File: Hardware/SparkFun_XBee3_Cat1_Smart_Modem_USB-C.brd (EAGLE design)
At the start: 53.3 x 59.7 mm, 105 parts, among them J3 USB Female Type C Connector, J4 QWIIC_RIGHT_ANGLE, U2 AP63203, U5 ESD Diode, U6 CP210X

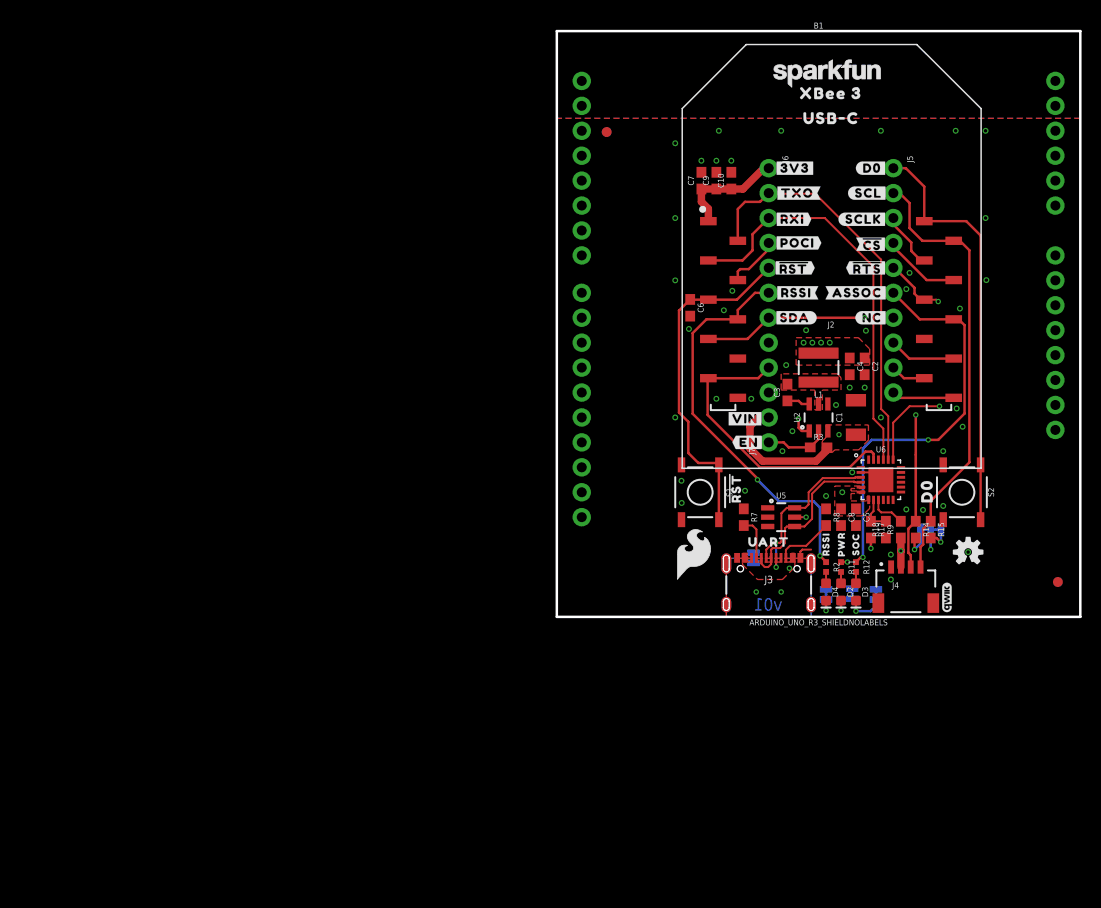
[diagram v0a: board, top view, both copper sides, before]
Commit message: General placement of parts
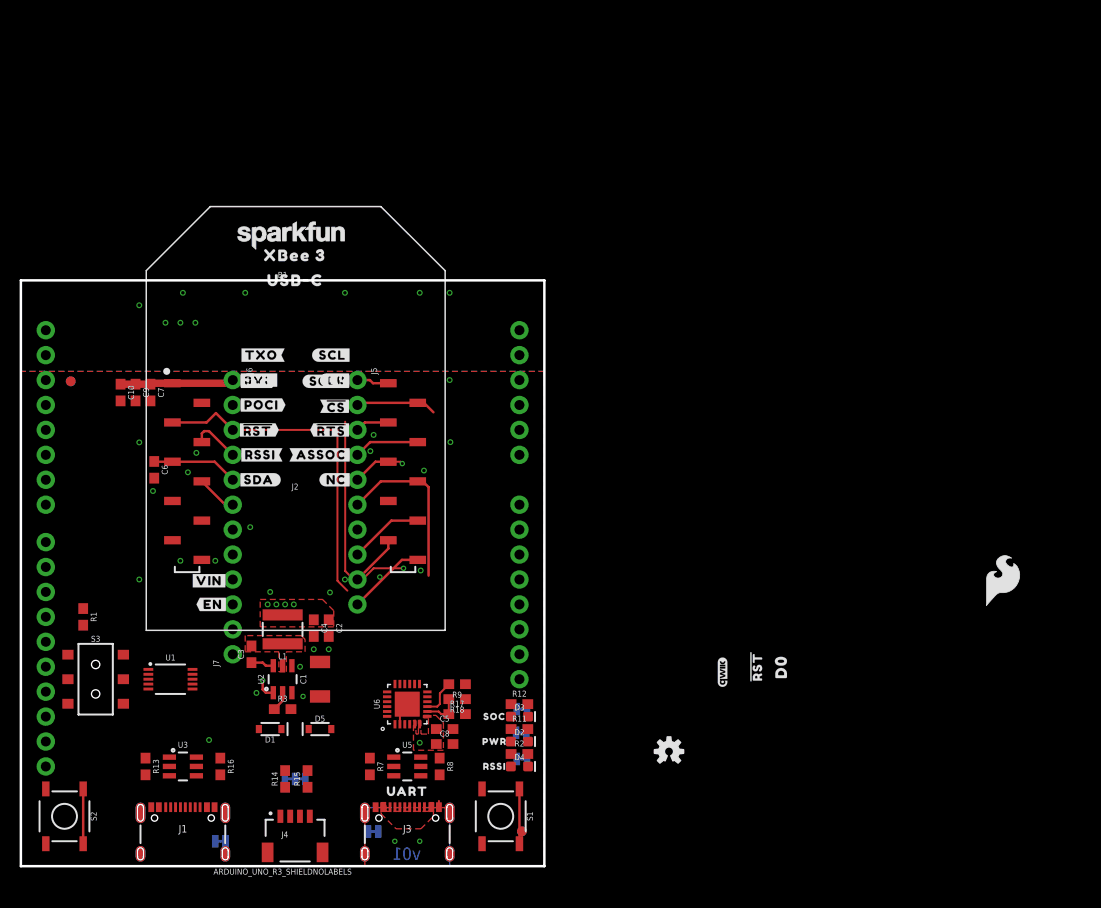
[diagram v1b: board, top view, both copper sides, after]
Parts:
- added D1, D5: 3A/10V/280mV, SparkFun-DiscreteSemi:SOD-323
- added J1: USB Female Type C Connector, SparkFun-Connectors:USB-C-16P-4LAYER-ISOLATED
- added R1: 100k, SparkFun-Resistors:0603
- added R13, R16: 5.1k, SparkFun-Resistors:0603
- added S3: (no value), SparkFun-Switches:SWITCH_DPDT_SMD_AYZ0202
- added SHLD1: JUMPER-SMT_2_NC_TRACE_SILK, SparkFun-Jumpers:SMT-JUMPER_2_NC_TRACE_SILK
- added U1: FSUSB30MUX_MSOP10, SparkFun-IC-Special-Function:MSOP10
- added U3: ESD Diode, SparkFun-DiscreteSemi:SOT-23-6
- R11, R12, R2: device SparkFun-Resistors:0402-TIGHT -> SparkFun-Resistors:0603
- moved S2 97.2 mm to (4.45, 5.08)
- moved I2C_PU 69.6 mm to (27.9, 8.89)
- moved U$26 69.6 mm to (27.9, 7.24)
- moved R14 69.1 mm to (26.9, 8.89), turned to 90 degrees
- moved R15 68.4 mm to (29.2, 8.89), turned to 90 degrees
- moved J4 67.2 mm to (27.9, 5.08)
- moved C10 65.9 mm to (10.2, 48.3), turned to 270 degrees
- moved C9 63.0 mm to (11.7, 48.3), turned to 270 degrees
- moved C1 60.8 mm to (30.5, 19.1)
- moved C2 60.8 mm to (31.4, 24.3)
- moved C3 60.8 mm to (23.5, 21.6)
- moved C4 60.8 mm to (29.8, 24.3)
- moved L1 60.8 mm to (26.7, 24.1)
- moved R3 60.8 mm to (26.7, 16.0)
- moved U2 60.8 mm to (26.7, 19.1)
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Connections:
- removed net N$17: B1.D12
- removed net N$20: B1.D9
- removed net N$22: B1.D8
- removed net N$24: B1.D7
- removed net N$25: B1.D6
- removed net N$4: J2.8
- new net DIRECT_D+: J1.A6, J1.B6, U1.3, U3.6
- new net DIRECT_D-: J1.A7, J1.B7, U1.7, U3.4
- new net DIRECT_SELECT: S3.2, S3.5, U1.1
- new net FIRMWARE: R1.2, S3.1, S3.4
- new net N$14: J1.B5, R16.2
- new net N$15: J1.A5, R13.2
- new net SHLD1: J1.SHLD1, J1.SHLD2, J1.SHLD3, J1.SHLD4, J1.SHLD5, J1.SHLD6, J1.SHLD7, J1.SHLD8, SHLD1.2
- new net V_USB_2: D1.A, J1.VBUS1, J1.VBUS2, U3.5
- new net XBEE_D+/SDA: J2.7, U1.4
- new net XBEE_D-: J2.8, U1.6
- net 3.3V: now also R1.1, U1.10
- net D11/SDA: now also U1.2; no longer J2.7
- net D12/SPI_POCI: now also B1.D12
- net D6/!RTS!: now also B1.D6
- net D7/!CTS!: now also B1.D7
- net D8/!DTR!: now also B1.D8
- net D9/!SLEEP!: now also B1.D9
- net GND: now also J1.GND, J1.GND2, R13.1, R16.1, S3.3, S3.6, SHLD1.1, U1.5, U1.9, U3.2
- net VIN: now also D1.C, D5.C
- net V_USB: now also D5.A
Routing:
- net D10/RSSI_PWM: track 53.1 -> 4.14 mm, vias 2 -> 0
- net D5/ASSOCIATE: track 58.2 -> 17.5 mm, vias 2 -> 0
- net D11/SDA: track 54.1 -> 13.9 mm, vias 2 -> 1
- net D1/SCL: track 46.0 -> 8.25 mm
- net D0: track 42.7 -> 8.87 mm
- net D8/!DTR!: track 30.8 -> 0.10 mm
- net D13/TXO: track 42.0 -> 16.2 mm
- net !RESET!: track 35.1 -> 14.6 mm
- net D+: track 19.5 -> 0.04 mm, vias 2 -> 0
- net VIN: track 29.3 -> 11.0 mm, vias 2 -> 1
- net D-: track 17.9 -> 0.15 mm
- net V_USB: track 7.08 -> 0.00 mm, vias 2 -> 0
- net D14/RXI: track 41.7 -> 34.7 mm
- net N$5: track 5.96 -> 0.00 mm
- net 3.3V: track 27.1 -> 21.7 mm, vias 9 -> 6
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- removed copper zone on layer 1, net VIN

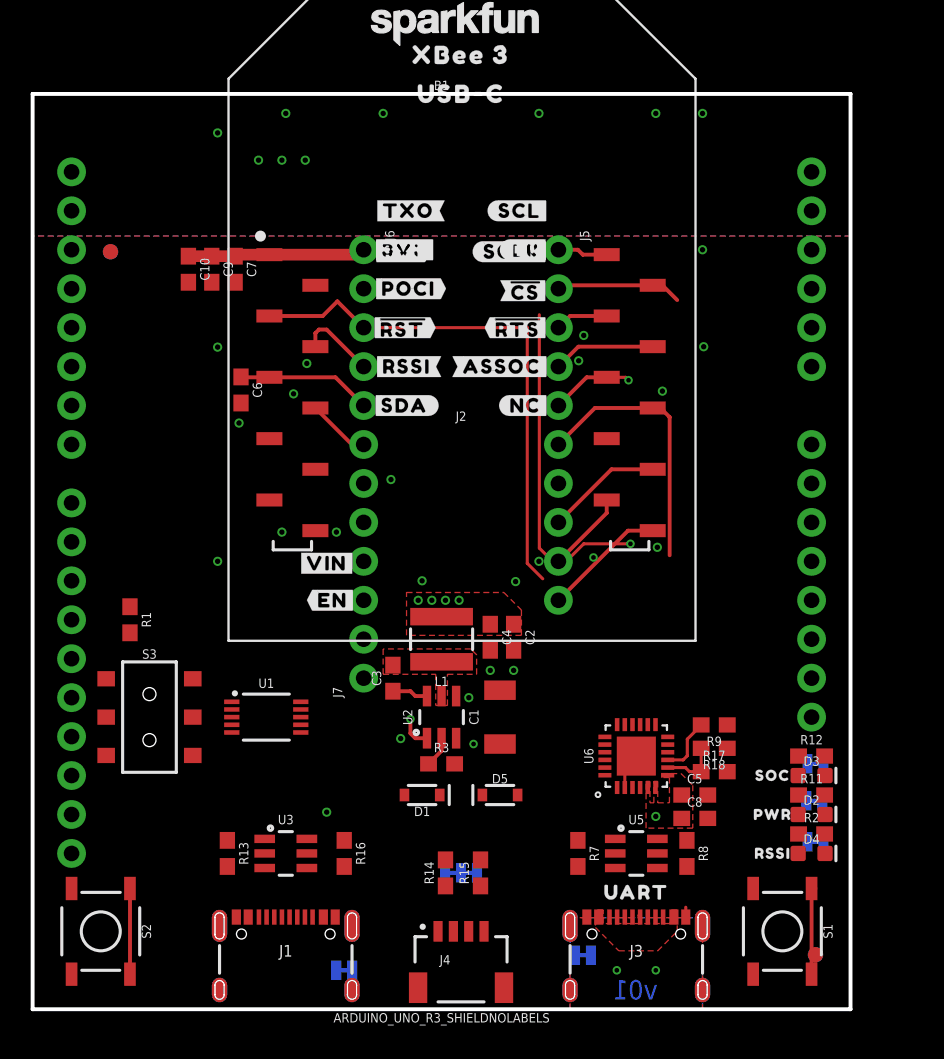
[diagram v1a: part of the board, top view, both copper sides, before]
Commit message: More changes to part placement
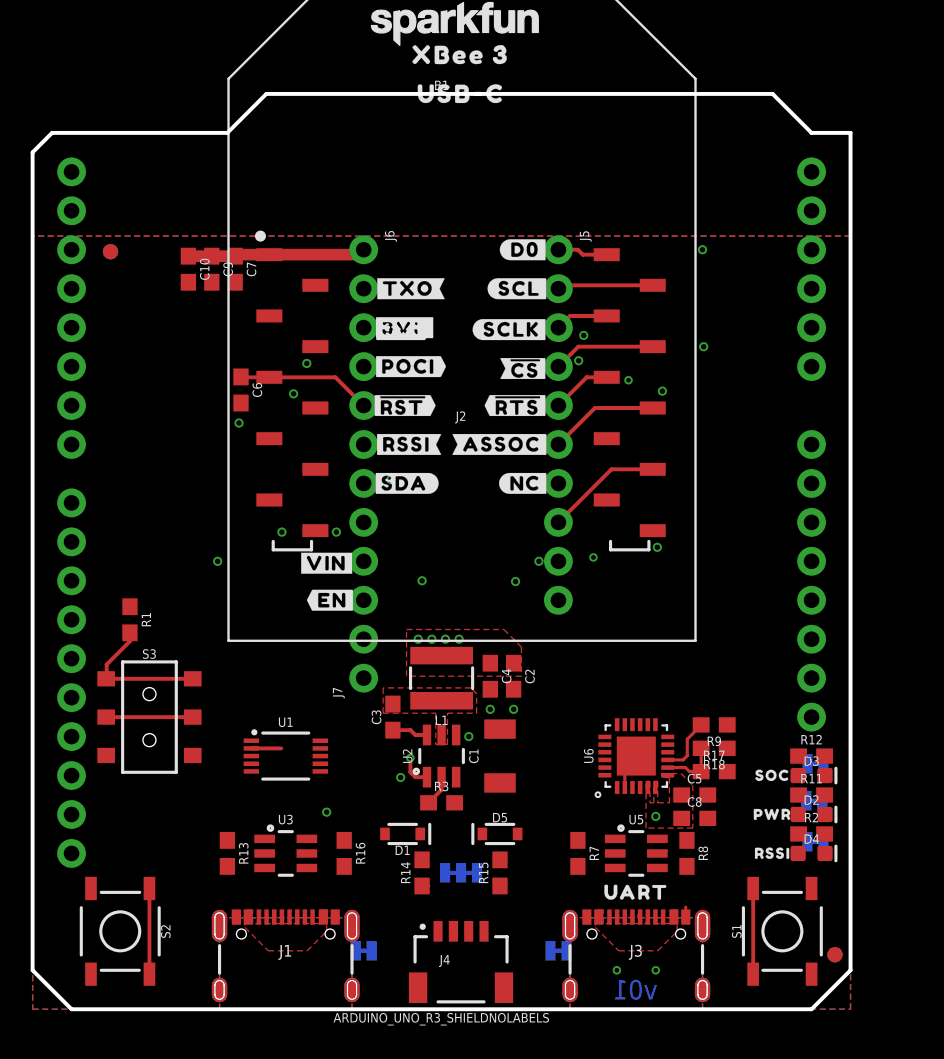
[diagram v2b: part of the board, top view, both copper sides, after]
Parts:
- moved U$45 5.08 mm to (24.5, 41.9)
- moved U$54 5.08 mm to (24.1, 39.4)
- moved U$58 5.08 mm to (31.6, 39.4)
- moved U$10 5.08 mm to (32.1, 34.3)
- moved U$21 5.08 mm to (24.5, 47.0)
- moved U$27 5.08 mm to (24.0, 44.3)
- moved U$55 5.08 mm to (24.4, 36.8)
- moved U$56 5.08 mm to (24.3, 34.3)
- moved U$57 5.08 mm to (30.6, 36.8)
- moved U$59 5.08 mm to (32.1, 41.8)
- moved U$60 5.08 mm to (31.2, 44.3)
- moved U$64 5.08 mm to (31.8, 47.0)
- moved U$9 5.08 mm to (24.3, 44.5)
- moved D1 2.84 mm to (24.1, 11.4)
- moved U1 2.84 mm to (16.5, 16.5)
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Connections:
- net N$27 renamed D4_SPI_PICO
- removed net N$16: B1.D13
- removed net N$28: B1.D3
- removed net N$29: B1.D2
- removed net N$35: B1.AREF
- removed net N$37: B1.5V
- removed net N$38: B1.VIN
- removed net N$39: B1.RES
- removed net N$40: B1.IOREF
- removed net N$41: B1.A5
- removed net N$42: B1.A4
- removed net N$43: B1.A3
- removed net N$44: B1.A2
- removed net N$45: B1.A1
- removed net N$46: B1.A0
- net D0: now also B1.A0
- net D11/SDA: no longer B1.D11
- net D2/SPI_CLK: now also B1.D2
- net D3/SPI_!CS!: now also B1.D3
- net VIN: now also B1.VIN
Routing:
- net D14/RXI: track 34.7 -> 0.00 mm
- net D6/!RTS!: track 21.5 -> 3.91 mm, vias 2 -> 1
- net D13/TXO: track 16.2 -> 0.00 mm
- net D11/SDA: track 13.9 -> 2.37 mm
- net VIN: track 11.0 -> 0.00 mm, vias 1 -> 0
- net D5/ASSOCIATE: track 17.5 -> 7.64 mm
- net FIRMWARE: track 0.00 -> 9.37 mm
- net D4/SPI_PICO: track 8.03 -> 0.00 mm
- net 3.3V: track 21.7 -> 13.8 mm
- net DIRECT_SELECT: track 0.00 -> 5.65 mm
- net D7/!CTS!: track 5.30 -> 0.00 mm
- net D12/SPI_POCI: track 5.13 -> 0.00 mm
- net D10/RSSI_PWM: track 4.14 -> 0.77 mm
- net D1/SCL: track 8.25 -> 6.89 mm
- net GND: vias 31 -> 21
- added copper zone on layer 1, net SHLD1
- added copper zone on layer 16, net SHLD1
- added copper zone on layer 1, net V_USB_2
- removed copper zone on layer 15, net 3.3V
- removed copper zone on layer 2, net GND
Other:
- outline, holes or cut-outs redrawn

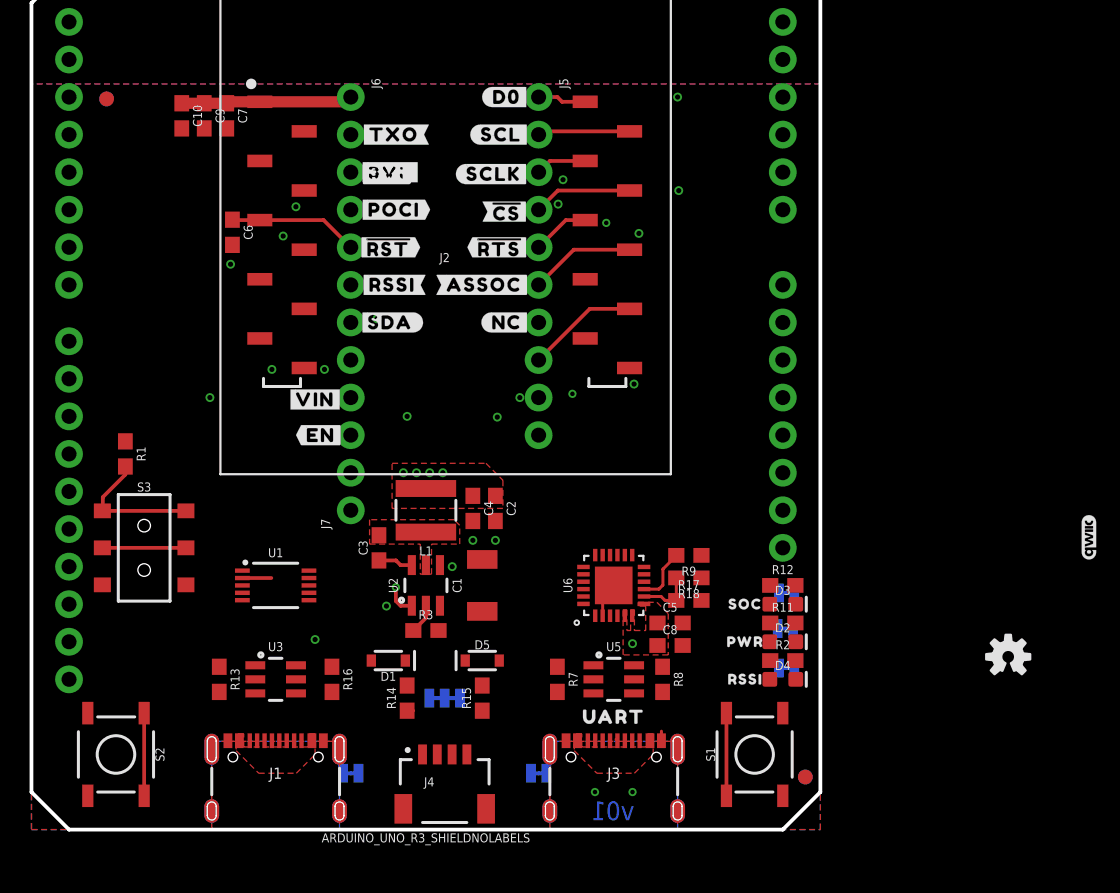
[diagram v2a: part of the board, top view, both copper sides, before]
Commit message: Rearranges USB-C and Qwiic connectors
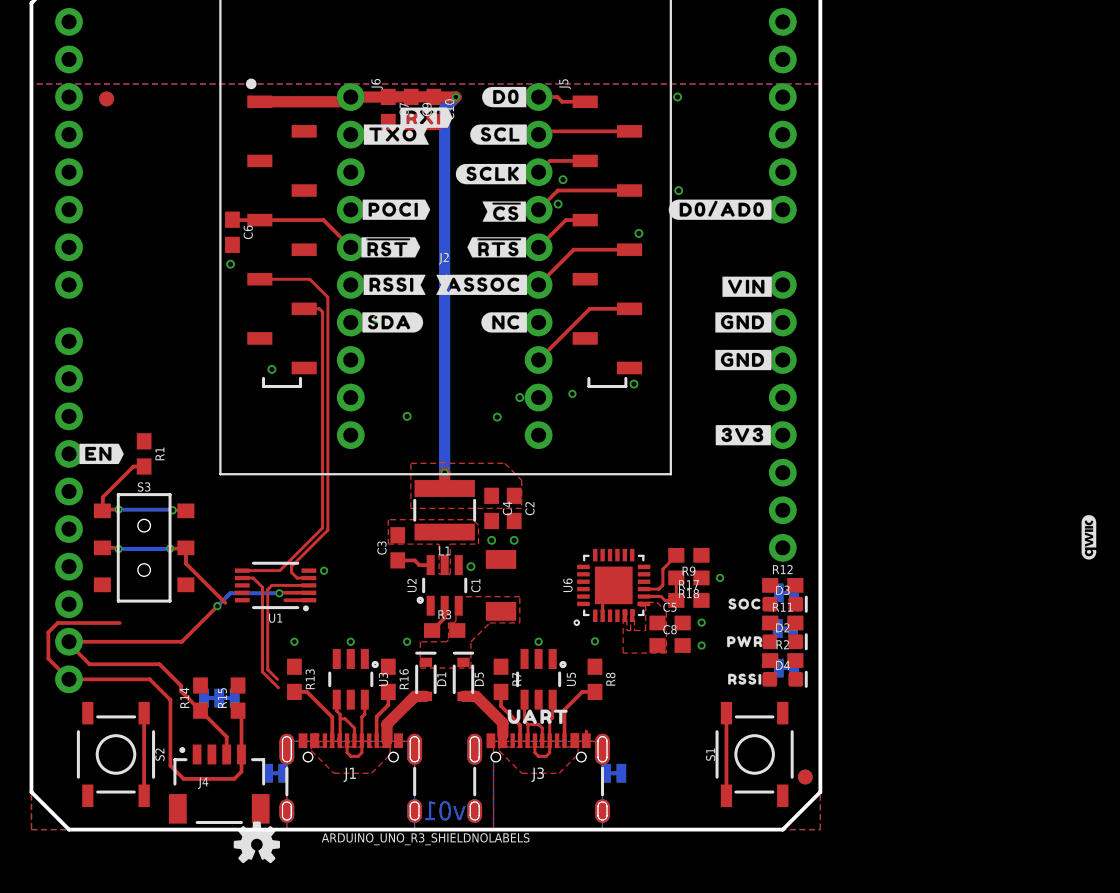
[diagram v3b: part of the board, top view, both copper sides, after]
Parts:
- removed J7: (no value), SparkFun-Connectors:1X02_NO_SILK
- removed U$46: (no value), top:#VIN#4
- removed U$67: (no value), botmirror:#EN#15
- removed U$9: (no value), top:#3V3#1
- added U$29: (no value), topmirror:#GND#0
- moved LOGO2 52.4 mm to (15.2, -1.02)
- moved U$44 40.4 mm to (48.1, 26.7), flipped to the top
- moved U$66 30.2 mm to (48.4, 36.7)
- moved U$12 29.2 mm to (48.1, 31.8), flipped to the top
- moved C10 17.0 mm to (27.2, 48.7)
- moved R15 16.5 mm to (14.0, 8.89)
- moved I2C_PU 15.2 mm to (12.7, 8.89)
- moved J4 15.2 mm to (12.7, 5.08)
- moved U$26 15.2 mm to (12.7, 7.24)
- moved U$8 15.2 mm to (46.7, 41.9), flipped to the top
- moved U$48 15.0 mm to (4.57, 25.4), flipped to the top
- moved C9 14.0 mm to (25.7, 48.7)
- moved R14 14.0 mm to (11.4, 8.89)
- moved C7 10.9 mm to (24.1, 48.7)
- moved R13 5.08 mm to (17.8, 10.2)
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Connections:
- net EN: now also B1.D11; no longer J7.1
- net VIN: no longer J7.2
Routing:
- net D1/SCL: track 6.89 -> 37.2 mm
- net D11/SDA: track 2.37 -> 32.4 mm, vias 1 -> 3
- net 3.3V: track 13.8 -> 40.4 mm, vias 6 -> 2
- net XBEE_D+/SDA: track 0.00 -> 26.1 mm
- net XBEE_D-: track 0.00 -> 22.6 mm
- net DIRECT_D+: track 0.00 -> 15.1 mm
- net DIRECT_D-: track 0.00 -> 13.9 mm
- net DIRECT_SELECT: track 5.65 -> 12.1 mm, vias 0 -> 2
- net D+: track 0.04 -> 6.15 mm
- net D-: track 0.15 -> 5.26 mm
- net N$15: track 0.00 -> 4.86 mm
- net N$5: track 0.00 -> 4.65 mm
- net V_USB_2: track 0.00 -> 4.53 mm
- net V_USB: track 0.00 -> 4.26 mm
- net N$6: track 0.00 -> 3.83 mm
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- added copper zone on layer 1, net VIN

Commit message: Routes some nets ( feels good now )
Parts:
- moved I2C_PU 1.27 mm to (12.7, 10.2)
- moved R14 1.27 mm to (11.4, 10.2)
- moved R15 1.27 mm to (14.0, 10.2)
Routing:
- net D1/SCL: track 37.2 -> 99.5 mm
- net D11/SDA: track 32.4 -> 52.8 mm, vias 3 -> 2
- net DIRECT_D+: track 15.1 -> 21.5 mm
- net DIRECT_SELECT: track 12.1 -> 5.71 mm
- net DIRECT_D-: track 13.9 -> 17.8 mm
- net GND: vias 24 -> 15

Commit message: Routes more stuff
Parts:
- moved C9 15.5 mm to (10.2, 48.3)
- moved C10 15.5 mm to (11.7, 48.3)
- moved C7 15.5 mm to (8.64, 48.3)
- moved R1 2.54 mm to (10.2, 25.4)
- moved SHLD 1.04 mm to (38.6, 3.07)
- moved SHLD1 0.92 mm to (17.2, 3.25)
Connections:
- removed net D4_SPI_PICO: B1.D4
- net D4/SPI_PICO: now also B1.D4
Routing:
- net EN: track 2.02 -> 36.8 mm, vias 0 -> 1
- net D5/ASSOCIATE: track 7.64 -> 36.2 mm
- net D8/!DTR!: track 0.10 -> 22.3 mm, vias 0 -> 1
- net DIRECT_SELECT: track 5.71 -> 22.6 mm, vias 2 -> 3
- net D0: track 8.87 -> 25.3 mm
- net D-: track 5.26 -> 16.0 mm, vias 0 -> 2
- net 3.3V: track 40.4 -> 31.1 mm, vias 2 -> 17
- net D+: track 6.15 -> 14.2 mm
- net D4/SPI_PICO: track 0.00 -> 8.03 mm
- net V_USB_2: track 4.53 -> 11.8 mm, vias 0 -> 2
- net V_USB: track 4.26 -> 11.6 mm, vias 0 -> 2
- net D14/RXI: track 0.00 -> 6.46 mm
- net D7/!CTS!: track 0.00 -> 5.30 mm
- net D12/SPI_POCI: track 0.00 -> 3.69 mm
- net D13/TXO: track 0.00 -> 3.55 mm
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- added copper zone on layer 15, net 3.3V
- added copper zone on layer 2, net GND
